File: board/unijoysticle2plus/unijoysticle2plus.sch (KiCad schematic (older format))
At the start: 35 parts, among them J1 DB9_Female, J2 DB9_Female, J3 Barrel_Jack, J4 Conn_01x03_Male, J5 USB_B_Micro, Q1 S8050, Q2 S8050, SW1 SW_Push, SW2 SW_SPST, SW3 SW_Push, SW4 SW_Push, U1 ESP32-WROOM-32D, U2 74LS05, U3 74LS05, U4 CP2102N-A01-GQFN24, U5 AP2114H-3_3TRG1

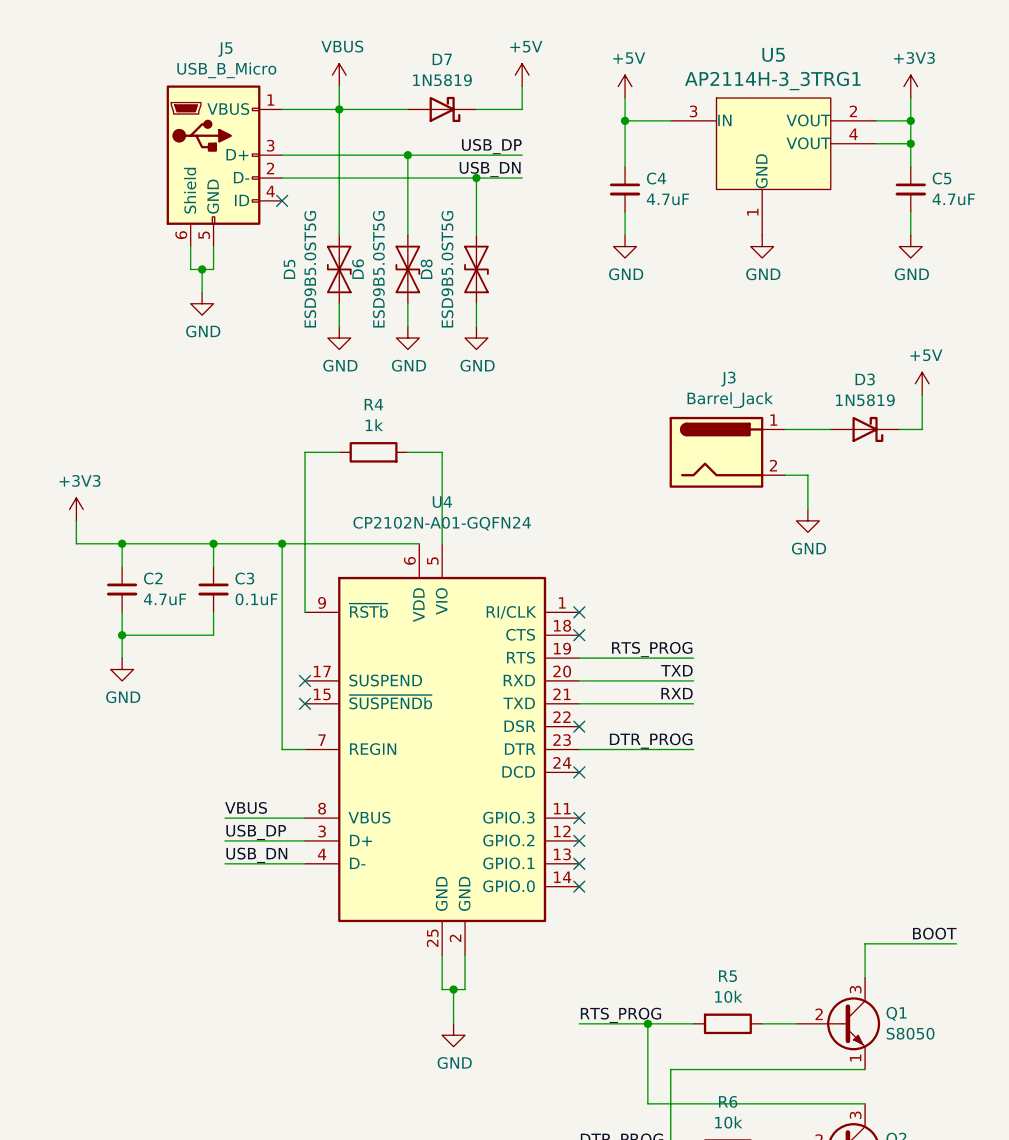
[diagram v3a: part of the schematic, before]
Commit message: unijoysticle2plus: more footprints
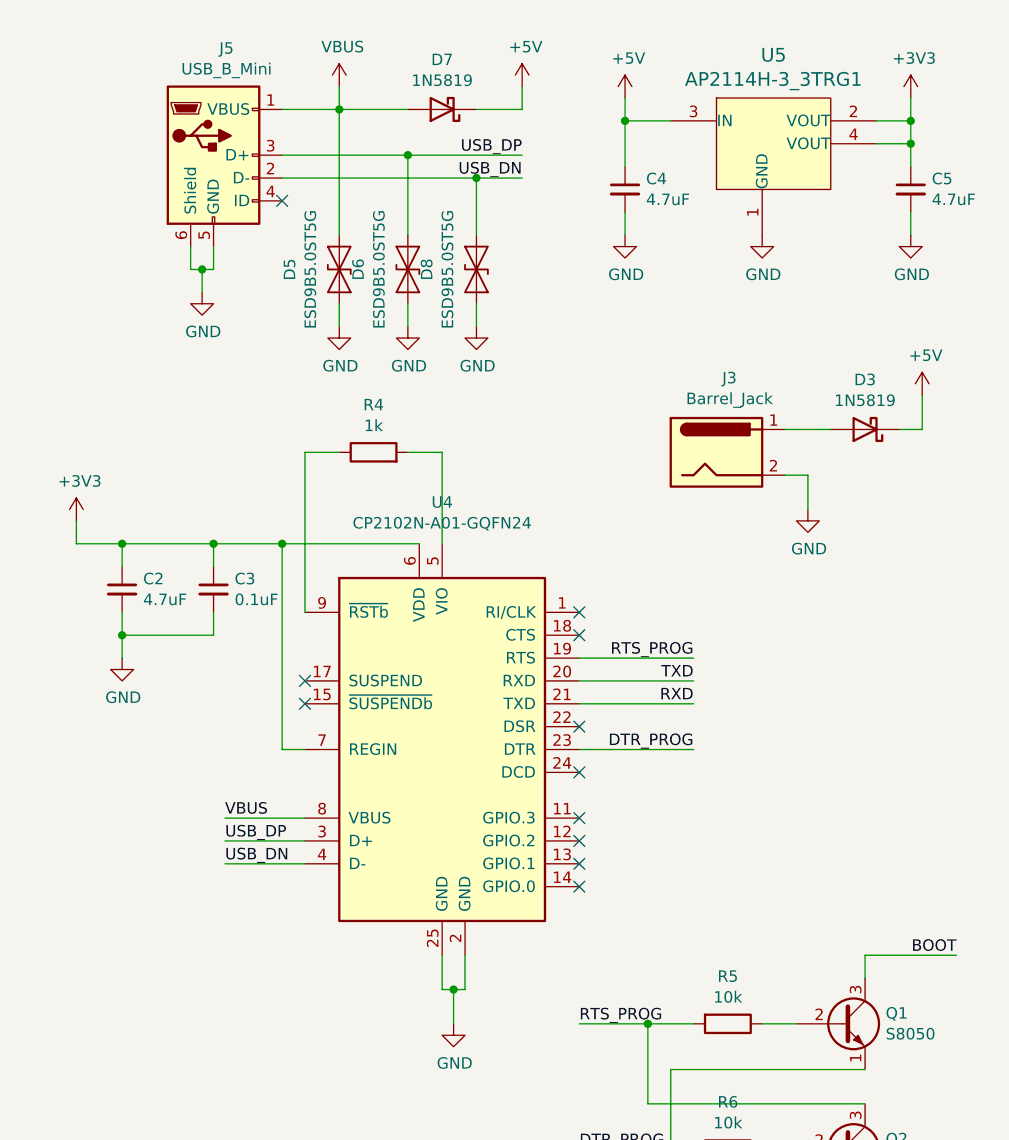
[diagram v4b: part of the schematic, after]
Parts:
- removed J5: USB_B_Micro, Connectors:USB-MICROB, symbol Connector:USB_B_Micro
- added J5: USB_B_Mini, Connectors:USB-MINIB, symbol Connector:USB_B_Mini
- C1, C2, C3, C4, C5: footprint (none) -> Capacitor_SMD:C_0805_2012Metric_Pad1.18x1.45mm_HandSolder
- D1, D2: footprint (none) -> LED_SMD:LED_0805_2012Metric_Pad1.15x1.40mm_HandSolder
- D3, D4: footprint (none) -> Diode_SMD:D_0805_2012Metric_Pad1.15x1.40mm_HandSolder
- D7: footprint Diode_THT:D_DO-41_SOD81_P10.16mm_Horizontal -> Diode_SMD:D_0805_2012Metric_Pad1.15x1.40mm_HandSolder
- J4: footprint (none) -> Connector_PinHeader_2.54mm:PinHeader_1x03_P2.54mm_Vertical
- SW1: footprint (none) -> Button_Switch_THT:SW_Tactile_SPST_Angled_PTS645Vx39-2LFS
- SW2: footprint (none) -> Button_Switch_THT:SW_CuK_OS102011MA1QN1_SPDT_Angled
- SW3, SW4: footprint (none) -> Button_Switch_THT:SW_Tactile_Straight_KSA0Axx1LFTR
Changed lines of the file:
@@
 F 0 "C1" H 4015 1596 50  0000 L CNN
 F 1 ".1uF" H 4015 1505 50  0000 L CNN
-F 2 "" H 3938 1400 50  0001 C CNN
+F 2 "Capacitor_SMD:C_0805_2012Metric_Pad1.18x1.45mm_HandSolder" H 3938 1400 50  0001 C CNN
 F 3 "~" H 3900 1550 50  0001 C CNN
 	1    3900 1550
@@
 F 0 "SW3" H 3850 2735 50  0000 C CNN
 F 1 "SW_Push" H 3850 2644 50  0000 C CNN
-F 2 "" H 3850 2650 50  0001 C CNN
+F 2 "Button_Switch_THT:SW_Tactile_Straight_KSA0Axx1LFTR" H 3850 2650 50  0001 C CNN
 F 3 "~" H 3850 2650 50  0001 C CNN
 	1    3850 2450
@@
 F 0 "SW4" H 6000 1685 50  0000 C CNN
 F 1 "SW_Push" H 6000 1594 50  0000 C CNN
-F 2 "" H 6000 1600 50  0001 C CNN
+F 2 "Button_Switch_THT:SW_Tactile_Straight_KSA0Axx1LFTR" H 6000 1600 50  0001 C CNN
 F 3 "~" H 6000 1600 50  0001 C CNN
 	1    6000 1400
@@
 F 0 "D4" H 1850 2933 50  0000 C CNN
 F 1 "1N5819" H 1850 3024 50  0000 C CNN
-F 2 "" H 1850 2975 50  0001 C CNN
+F 2 "Diode_SMD:D_0805_2012Metric_Pad1.15x1.40mm_HandSolder" H 1850 2975 50  0001 C CNN
 F 3 "http://www.vishay.com/docs/88525/1n5817.pdf" H 1850 3150 50  0001 C CNN
 	1    1850 3150
@@
 F 0 "SW2" H 2300 3385 50  0000 C CNN
 F 1 "SW_SPST" H 2300 3294 50  0000 C CNN
-F 2 "" H 2300 3150 50  0001 C CNN
+F 2 "Button_Switch_THT:SW_CuK_OS102011MA1QN1_SPDT_Angled" H 2300 3150 50  0001 C CNN
 F 3 "~" H 2300 3150 50  0001 C CNN
 	1    2300 3150
@@
 F 0 "D1" H 4843 7067 50  0000 C CNN
 F 1 "LED" H 4843 6976 50  0000 C CNN
-F 2 "" H 4850 6850 50  0001 C CNN
+F 2 "LED_SMD:LED_0805_2012Metric_Pad1.15x1.40mm_HandSolder" H 4850 6850 50  0001 C CNN
 F 3 "~" H 4850 6850 50  0001 C CNN
 	1    4850 6850
@@
 F 0 "D2" H 4843 7367 50  0000 C CNN
 F 1 "LED" H 4843 7276 50  0000 C CNN
-F 2 "" H 4850 7150 50  0001 C CNN
+F 2 "LED_SMD:LED_0805_2012Metric_Pad1.15x1.40mm_HandSolder" H 4850 7150 50  0001 C CNN
 F 3 "~" H 4850 7150 50  0001 C CNN
 	1    4850 7150
@@
 F 0 "SW1" H 4900 7735 50  0000 C CNN
 F 1 "SW_Push" H 4900 7644 50  0000 C CNN
-F 2 "" H 4900 7650 50  0001 C CNN
+F 2 "Button_Switch_THT:SW_Tactile_SPST_Angled_PTS645Vx39-2LFS" H 4900 7650 50  0001 C CNN
 F 3 "~" H 4900 7650 50  0001 C CNN
 	1    4900 7450
@@
 F 0 "D3" H 10700 2033 50  0000 C CNN
 F 1 "1N5819" H 10700 2124 50  0000 C CNN
-F 2 "" H 10700 2075 50  0001 C CNN
+F 2 "Diode_SMD:D_0805_2012Metric_Pad1.15x1.40mm_HandSolder" H 10700 2075 50  0001 C CNN
 F 3 "http://www.vishay.com/docs/88525/1n5817.pdf" H 10700 2250 50  0001 C CNN
 	1    10700 2250
@@
 F 0 "D7" H 8850 633 50  0000 C CNN
 F 1 "1N5819" H 8850 724 50  0000 C CNN
-F 2 "Diode_THT:D_DO-41_SOD81_P10.16mm_Horizontal" H 8850 675 50  0001 C CNN
+F 2 "Diode_SMD:D_0805_2012Metric_Pad1.15x1.40mm_HandSolder" H 8850 675 50  0001 C CNN
 F 3 "http://www.vishay.com/docs/88525/1n5817.pdf" H 8850 850 50  0001 C CNN
 	1    8850 850
@@
 F 0 "C2" H 7542 2996 50  0000 L CNN
 F 1 "4.7uF" H 7542 2905 50  0000 L CNN
-F 2 "" H 7450 2950 50  0001 C CNN
+F 2 "Capacitor_SMD:C_0805_2012Metric_Pad1.18x1.45mm_HandSolder" H 7450 2950 50  0001 C CNN
 F 3 "~" H 7450 2950 50  0001 C CNN
 	1    7450 2950
@@
 F 0 "C3" H 7942 2996 50  0000 L CNN
 F 1 "0.1uF" H 7942 2905 50  0000 L CNN
-F 2 "" H 7850 2950 50  0001 C CNN
+F 2 "Capacitor_SMD:C_0805_2012Metric_Pad1.18x1.45mm_HandSolder" H 7850 2950 50  0001 C CNN
 F 3 "~" H 7850 2950 50  0001 C CNN
 	1    7850 2950
@@
 F 0 "J4" H 4708 6231 50  0000 C CNN
 F 1 "Conn_01x03_Male" H 4708 6140 50  0000 C CNN
-F 2 "" H 4600 5950 50  0001 C CNN
+F 2 "Connector_PinHeader_2.54mm:PinHeader_1x03_P2.54mm_Vertical" H 4600 5950 50  0001 C CNN
 F 3 "~" H 4600 5950 50  0001 C CNN
 	1    4600 5950
@@
 F 0 "C4" H 9742 1246 50  0000 L CNN
 F 1 "4.7uF" H 9742 1155 50  0000 L CNN
-F 2 "" H 9650 1200 50  0001 C CNN
+F 2 "Capacitor_SMD:C_0805_2012Metric_Pad1.18x1.45mm_HandSolder" H 9650 1200 50  0001 C CNN
 F 3 "~" H 9650 1200 50  0001 C CNN
 	1    9650 1200
@@
 F 0 "C5" H 10992 1246 50  0000 L CNN
 F 1 "4.7uF" H 10992 1155 50  0000 L CNN
-F 2 "" H 10900 1200 50  0001 C CNN
+F 2 "Capacitor_SMD:C_0805_2012Metric_Pad1.18x1.45mm_HandSolder" H 10900 1200 50  0001 C CNN
 F 3 "~" H 10900 1200 50  0001 C CNN
 	1    10900 1200
@@
 F 3 "" H 9650 800 50  0001 C CNN
 	1    9650 800
-	1    0    0    -1
-$EndComp
-$Comp
-L Connector:USB_B_Micro J5
-U 1 1 609C412E
-P 7850 1050
-F 0 "J5" H 7907 1517 50  0000 C CNN
-F 1 "USB_B_Micro" H 7907 1426 50  0000 C CNN
-F 2 "Connectors:USB-MICROB" H 8000 1000 50  0001 C CNN
-F 3 "~" H 8000 1000 50  0001 C CNN
-	1    7850 1050
 	1    0    0    -1
 $EndComp
@@
 $EndComp
 Wire Wire Line
-	10700 4650 10700 4500
-Wire Wire Line
-	10700 4500 11100 4500
-Wire Wire Line
 	10700 5600 10700 5750
 Wire Wire Line
 	10700 5750 11100 5750
-Text Label 11100 4500 2    50   ~ 0
-BOOT
 Text Label 11100 5750 2    50   ~ 0
 RESET
@@
 	1    0    0    -1
 $EndComp
+Wire Wire Line
+	10700 4650 10700 4550
+Wire Wire Line
+	10700 4550 11100 4550
+Text Label 11100 4550 2    50   ~ 0
+BOOT
+$Comp
+L Connector:USB_B_Mini J5
+U 1 1 5FAFDC89
+P 7850 1050
+F 0 "J5" H 7907 1517 50  0000 C CNN
+F 1 "USB_B_Mini" H 7907 1426 50  0000 C CNN
+F 2 "Connectors:USB-MINIB" H 8000 1000 50  0001 C CNN
+F 3 "~" H 8000 1000 50  0001 C CNN
+	1    7850 1050
+	1    0    0    -1
+$EndComp

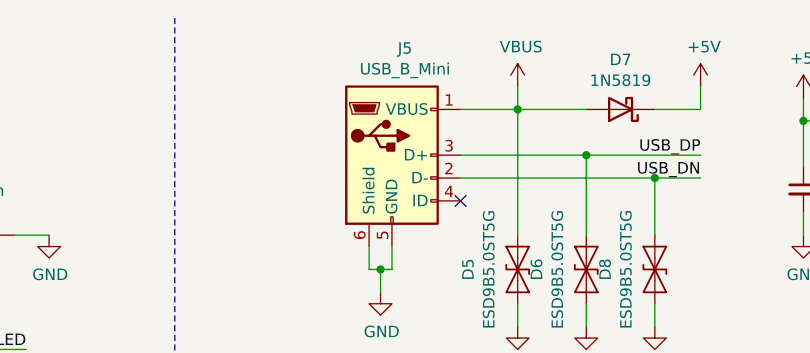
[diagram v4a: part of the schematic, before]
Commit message: unijoysticle2plus: usb micro footprint connected
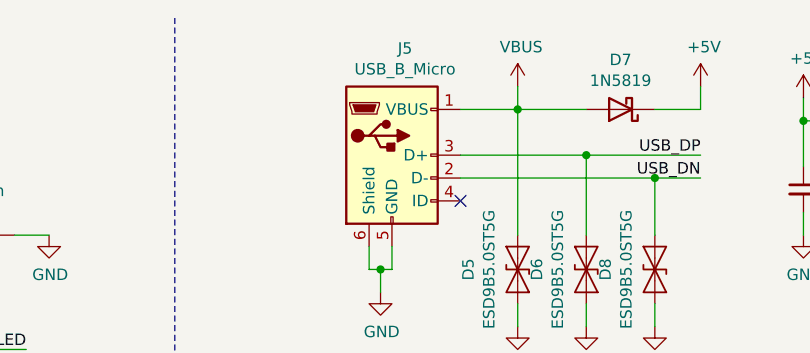
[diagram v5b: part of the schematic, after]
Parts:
- removed J5: USB_B_Mini, Connectors:USB-MINIB, symbol Connector:USB_B_Mini
- added J5: USB_B_Micro, Connector_USB:USB_Micro-B_Molex-105017-0001, symbol Connector:USB_B_Micro
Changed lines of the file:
@@
 BOOT
 $Comp
-L Connector:USB_B_Mini J5
-U 1 1 5FAFDC89
+L Connector:USB_B_Micro J5
+U 1 1 5F99FD12
 P 7850 1050
 F 0 "J5" H 7907 1517 50  0000 C CNN
-F 1 "USB_B_Mini" H 7907 1426 50  0000 C CNN
-F 2 "Connectors:USB-MINIB" H 8000 1000 50  0001 C CNN
+F 1 "USB_B_Micro" H 7907 1426 50  0000 C CNN
+F 2 "Connector_USB:USB_Micro-B_Molex-105017-0001" H 8000 1000 50  0001 C CNN
 F 3 "~" H 8000 1000 50  0001 C CNN
 	1    7850 1050

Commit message: Firmware cleanup: remove obsolte files
Remove Changelog/License related to firmware
Remove code files from .gitignore
  Ignore fp-info-cache (kicad  file)
Update docs like pair_ds3 which points to Bluepad32

Regarding Unijoysticle2Plus: non important changes... this is still
pretty much WIP, so just ignore these changes
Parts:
- removed C2: 4.7uF, Capacitor_SMD:C_0805_2012Metric_Pad1.18x1.45mm_HandSolder, symbol Device:C_Small
- removed C3: 0.1uF, Capacitor_SMD:C_0805_2012Metric_Pad1.18x1.45mm_HandSolder, symbol Device:C_Small
- removed R4: 1k, Resistor_SMD:R_0805_2012Metric_Pad1.20x1.40mm_HandSolder, symbol Device:R
- removed U4: CP2102N-A01-GQFN24, Package_DFN_QFN:QFN-24-1EP_4x4mm_P0.5mm_EP2.6x2.6mm, symbol Interface_USB:CP2102N-A01-GQFN24
- added C?: 0.1uF, symbol Device:C_Small
- added R?: 1k, symbol Device:R_Small
- added U4: MCP2200-I-SO, Package_SO:SOIC-20W_7.5x12.8mm_P1.27mm, symbol Interface_USB:MCP2200-I-SO
- added U?: MCP2221AxSL, Package_SO:SOIC-14_3.9x8.7mm_P1.27mm, symbol Interface_USB:MCP2221AxSL
- added Y?: 12Mhz, symbol Device:Resonator_Small
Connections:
- net labels added: RDX, USBD+, USBD-
- net labels removed: USB_DN, USB_DP
- wire segments 184 -> 172
- no-connect marks 11 -> 1

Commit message: unijoysticle2 plus: using ch340c (WIP)
After researching which could be the cheapest way to create a board that
could be assembled by JLCPCB, it seems that using CH340C is the way to
go:

- CH340C is an extended part, but doesn't require oscillator. Cost: $0.5
- CH340G is a basic part, but requires 12Mhz oscillar, which is an
  external part.
- CP210x, are all external parts and cost > $2

So, the design will include a CH340C.

Schematic is "ready", but layout is not.
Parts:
- removed C?: 0.1uF, symbol Device:C_Small
- removed R?: 1k, symbol Device:R_Small
- removed U4: MCP2200-I-SO, Package_SO:SOIC-20W_7.5x12.8mm_P1.27mm, symbol Interface_USB:MCP2200-I-SO
- removed U?: MCP2221AxSL, Package_SO:SOIC-14_3.9x8.7mm_P1.27mm, symbol Interface_USB:MCP2221AxSL
- removed Y?: 12Mhz, symbol Device:Resonator_Small
- added C2, C3: .1uF, Capacitor_SMD:C_0805_2012Metric_Pad1.18x1.45mm_HandSolder, symbol Device:C_Small
- added U4: CH340C, Package_SO:SOIC-16_3.9x9.9mm_P1.27mm, symbol Interface_USB:CH340C
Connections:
- net labels added: ESP_RXD, ESP_TXD
- net labels removed: RDX, RXD, TXD
- wire segments 172 -> 171
- no-connect marks 1 -> 6
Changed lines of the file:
@@
 	5450 1700 5900 1700
 Text Label 5900 1500 2    50   ~ 0
-TXD
+ESP_TXD
 Text Label 5900 1700 2    50   ~ 0
-RXD
+ESP_RXD
 Wire Wire Line
 	5450 1800 5900 1800
@@
 	1    0    0    -1
 $EndComp
-Wire Wire Line
-	9300 2950 9750 2950
-Wire Wire Line
-	9300 3150 9750 3150
-Text Label 9750 2950 2    50   ~ 0
+$Comp
+L Interface_USB:CH340C U4
+U 1 1 60DA1496
+P 8000 3450
+F 0 "U4" H 7600 2900 50  0000 C CNN
+F 1 "CH340C" H 7650 2800 50  0000 C CNN
+F 2 "Package_SO:SOIC-16_3.9x9.9mm_P1.27mm" H 8050 2900 50  0001 L CNN
+F 3 "https://datasheet.lcsc.com/szlcsc/Jiangsu-Qin-Heng-CH340C_C84681.pdf" H 7650 4250 50  0001 C CNN
+	1    8000 3450
+	1    0    0    -1
+$EndComp
+Wire Wire Line
+	8400 3050 8850 3050
+Text Label 8550 3050 0    50   ~ 0
+ESP_RXD
+Wire Wire Line
+	8400 3150 8850 3150
+Text Label 8550 3150 0    50   ~ 0
+ESP_TXD
+Wire Wire Line
+	8400 3750 8850 3750
+Wire Wire Line
+	8400 3850 8850 3850
+Text Label 8500 3750 0    50   ~ 0
+DTR_PROG
+Text Label 8500 3850 0    50   ~ 0
+RTS_PROG
+NoConn ~ 8400 3350
+NoConn ~ 8400 3450
+NoConn ~ 8400 3550
+NoConn ~ 8400 3650
+NoConn ~ 7600 3150
+Wire Wire Line
+	7600 3350 7300 3350
+Wire Wire Line
+	7600 3450 7300 3450
+Text Label 7300 3350 0    50   ~ 0
 USBD+
-Text Label 9750 3150 2    50   ~ 0
+Text Label 7300 3450 0    50   ~ 0
 USBD-
-$Comp
-L Device:Resonator_Small Y?
-U 1 1 5FA8F467
-P 9600 4050
-F 0 "Y?" V 9925 4000 50  0000 C CNN
-F 1 "12Mhz" V 9834 4000 50  0000 C CNN
-F 2 "" H 9575 4050 50  0001 C CNN
-F 3 "~" H 9575 4050 50  0001 C CNN
-	1    9600 4050
-	0    -1   -1   0
-$EndComp
-Wire Wire Line
-	9300 3950 9500 3950
-Wire Wire Line
-	9300 4150 9500 4150
-Wire Wire Line
-	9800 4050 9900 4050
-Wire Wire Line
-	9900 4050 9900 4150
-$Comp
-L power:GND #PWR?
-U 1 1 5FAA7D92
-P 9900 4150
-F 0 "#PWR?" H 9900 3900 50  0001 C CNN
-F 1 "GND" H 9905 3977 50  0000 C CNN
-F 2 "" H 9900 4150 50  0001 C CNN
-F 3 "" H 9900 4150 50  0001 C CNN
-	1    9900 4150
-	1    0    0    -1
-$EndComp
-Wire Wire Line
-	7500 3050 7150 3050
-Wire Wire Line
-	7500 3150 7150 3150
-Text Label 7150 3050 0    50   ~ 0
-TXD
-Text Label 7150 3150 0    50   ~ 0
-RDX
-Wire Wire Line
-	8300 2400 8300 2500
-$Comp
-L power:VBUS #PWR?
-U 1 1 5FACC346
-P 8300 2400
-F 0 "#PWR?" H 8300 2250 50  0001 C CNN
-F 1 "VBUS" H 8315 2573 50  0000 C CNN
-F 2 "" H 8300 2400 50  0001 C CNN
-F 3 "" H 8300 2400 50  0001 C CNN
-	1    8300 2400
-	1    0    0    -1
-$EndComp
-Wire Wire Line
-	8300 2500 8100 2500
-Connection ~ 8300 2500
-Wire Wire Line
-	8300 2500 8300 2750
-Wire Wire Line
-	8400 4350 8400 4650
-$Comp
-L power:GND #PWR?
-U 1 1 5FB1E143
-P 8400 4650
-F 0 "#PWR?" H 8400 4400 50  0001 C CNN
-F 1 "GND" H 8405 4477 50  0000 C CNN
-F 2 "" H 8400 4650 50  0001 C CNN
-F 3 "" H 8400 4650 50  0001 C CNN
-	1    8400 4650
-	1    0    0    -1
-$EndComp
-$Comp
-L Device:C_Small C?
-U 1 1 5FB5A3AE
-P 8000 2500
-F 0 "C?" V 7771 2500 50  0000 C CNN
-F 1 "0.1uF" V 7862 2500 50  0000 C CNN
-F 2 "" H 8000 2500 50  0001 C CNN
-F 3 "~" H 8000 2500 50  0001 C CNN
-	1    8000 2500
+Wire Wire Line
+	8000 4050 8000 4150
+$Comp
+L power:GND #PWR0111
+U 1 1 60E6428D
+P 8000 4150
+F 0 "#PWR0111" H 8000 3900 50  0001 C CNN
+F 1 "GND" H 8005 3977 50  0000 C CNN
+F 2 "" H 8000 4150 50  0001 C CNN
+F 3 "" H 8000 4150 50  0001 C CNN
+	1    8000 4150
+	1    0    0    -1
+$EndComp
+Wire Wire Line
+	7900 2850 7900 2650
+Wire Wire Line
+	8000 2850 8000 2650
+Wire Wire Line
+	7900 2650 7800 2650
+Wire Wire Line
+	7600 2650 7350 2650
+Wire Wire Line
+	7350 2650 7350 2700
+$Comp
+L power:GND #PWR0125
+U 1 1 60E88C4A
+P 7350 2700
+F 0 "#PWR0125" H 7350 2450 50  0001 C CNN
+F 1 "GND" H 7355 2527 50  0000 C CNN
+F 2 "" H 7350 2700 50  0001 C CNN
+F 3 "" H 7350 2700 50  0001 C CNN
+	1    7350 2700
+	1    0    0    -1
+$EndComp
+Wire Wire Line
+	8300 2650 8650 2650
+Wire Wire Line
+	8650 2650 8650 2700
+$Comp
+L power:GND #PWR0132
+U 1 1 60EAC607
+P 8650 2700
+F 0 "#PWR0132" H 8650 2450 50  0001 C CNN
+F 1 "GND" H 8655 2527 50  0000 C CNN
+F 2 "" H 8650 2700 50  0001 C CNN
+F 3 "" H 8650 2700 50  0001 C CNN
+	1    8650 2700
+	1    0    0    -1
+$EndComp
+Wire Wire Line
+	8000 2650 8100 2650
+Wire Wire Line
+	8650 2650 8650 2550
+Connection ~ 8650 2650
+$Comp
+L power:+5V #PWR0126
+U 1 1 60EC4654
+P 8650 2550
+F 0 "#PWR0126" H 8650 2400 50  0001 C CNN
+F 1 "+5V" H 8665 2723 50  0000 C CNN
+F 2 "" H 8650 2550 50  0001 C CNN
+F 3 "" H 8650 2550 50  0001 C CNN
+	1    8650 2550
+	1    0    0    -1
+$EndComp
+$Comp
+L Device:C_Small C2
+U 1 1 60EF6BA5
+P 7700 2650
+F 0 "C2" V 7471 2650 50  0000 C CNN
+F 1 ".1uF" V 7562 2650 50  0000 C CNN
+F 2 "Capacitor_SMD:C_0805_2012Metric_Pad1.18x1.45mm_HandSolder" H 7700 2650 50  0001 C CNN
+F 3 "~" H 7700 2650 50  0001 C CNN
+	1    7700 2650
 	0    1    1    0
 $EndComp
-Wire Wire Line
-	7900 2500 7900 2550
-$Comp
-L power:GND #PWR?
-U 1 1 5FB64A2F
-P 7900 2550
-F 0 "#PWR?" H 7900 2300 50  0001 C CNN
-F 1 "GND" H 7905 2377 50  0000 C CNN
-F 2 "" H 7900 2550 50  0001 C CNN
-F 3 "" H 7900 2550 50  0001 C CNN
-	1    7900 2550
-	1    0    0    -1
-$EndComp
-$Comp
-L Interface_USB:MCP2200-I-SO U4
-U 1 1 5F9EDB53
-P 8400 3550
-F 0 "U4" H 8400 2661 50  0000 C CNN
-F 1 "MCP2200-I-SO" H 8400 2570 50  0000 C CNN
-F 2 "Package_SO:SOIC-20W_7.5x12.8mm_P1.27mm" H 8400 2400 50  0001 C CNN
-F 3 "http://ww1.microchip.com/downloads/en/DeviceDoc/200022228D.pdf" H 8400 2550 50  0001 C CNN
-	1    8400 3550
-	1    0    0    -1
-$EndComp
-Wire Wire Line
-	8500 2500 8500 2750
-Wire Wire Line
-	7500 2950 7150 2950
-Wire Wire Line
-	7150 2950 7150 2800
-$Comp
-L Device:R_Small R?
-U 1 1 5FBBC5FE
-P 7150 2700
-F 0 "R?" H 7209 2746 50  0000 L CNN
-F 1 "1k" H 7209 2655 50  0000 L CNN
-F 2 "" H 7150 2700 50  0001 C CNN
-F 3 "~" H 7150 2700 50  0001 C CNN
-	1    7150 2700
-	1    0    0    -1
-$EndComp
-Wire Wire Line
-	7150 2600 7150 2550
-$Comp
-L power:VBUS #PWR?
-U 1 1 5FBC6994
-P 7150 2550
-F 0 "#PWR?" H 7150 2400 50  0001 C CNN
-F 1 "VBUS" H 7165 2723 50  0000 C CNN
-F 2 "" H 7150 2550 50  0001 C CNN
-F 3 "" H 7150 2550 50  0001 C CNN
-	1    7150 2550
-	1    0    0    -1
-$EndComp
-$Comp
-L Interface_USB:MCP2221AxSL U?
-U 1 1 5FBDB3F3
-P 7600 5250
-F 0 "U?" H 7600 4561 50  0000 C CNN
-F 1 "MCP2221AxSL" H 7600 4470 50  0000 C CNN
-F 2 "Package_SO:SOIC-14_3.9x8.7mm_P1.27mm" H 7600 6250 50  0001 C CNN
-F 3 "http://ww1.microchip.com/downloads/en/DeviceDoc/20005565B.pdf" H 7600 5950 50  0001 C CNN
-	1    7600 5250
-	1    0    0    -1
+$Comp
+L Device:C_Small C3
+U 1 1 60EF76EE
+P 8200 2650
+F 0 "C3" V 7971 2650 50  0000 C CNN
+F 1 ".1uF" V 8062 2650 50  0000 C CNN
+F 2 "Capacitor_SMD:C_0805_2012Metric_Pad1.18x1.45mm_HandSolder" H 8200 2650 50  0001 C CNN
+F 3 "~" H 8200 2650 50  0001 C CNN
+	1    8200 2650
+	0    1    1    0
 $EndComp
 $EndSCHEMATC
